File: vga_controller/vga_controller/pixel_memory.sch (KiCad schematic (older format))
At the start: 7 parts, among them J1 DB15_Female_HighDensity

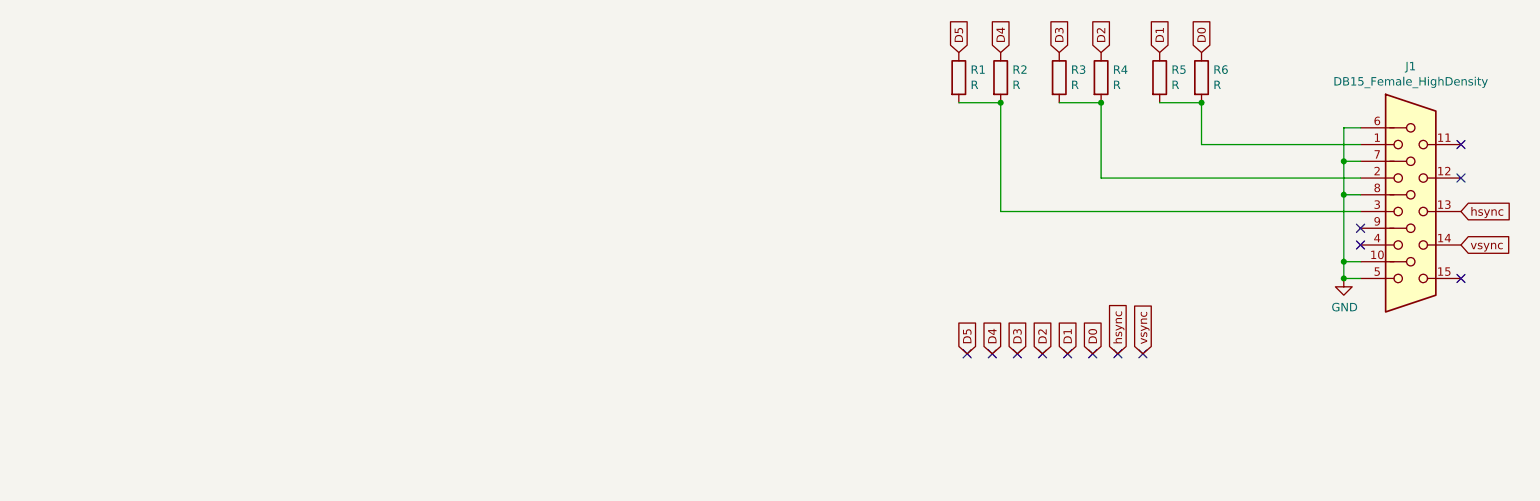
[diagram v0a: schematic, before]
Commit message: made interconnections between sheets
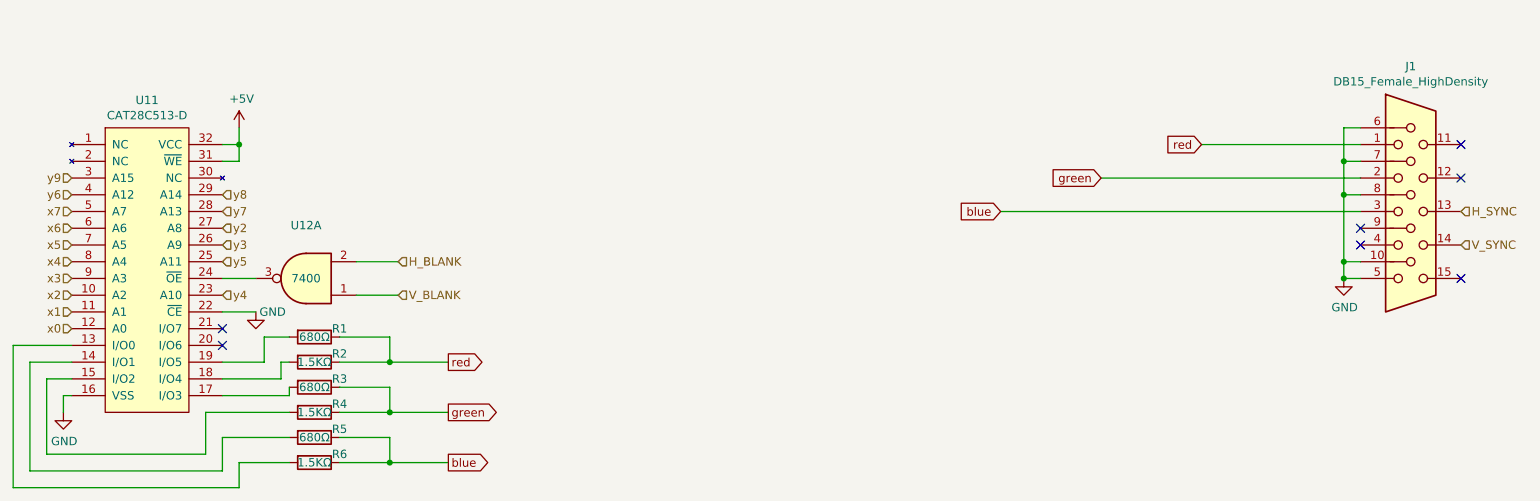
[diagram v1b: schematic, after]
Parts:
- added U11: CAT28C513-D, Package_DIP:DIP-32_W7.62mm, symbol vga_controller-rescue:CAT28C513-D-parallel_eeprom
- added U12: 7400, symbol 74xx:7400
- R1, R3, R5: value R -> 680Ω
- R2, R4, R6: value R -> 1.5KΩ
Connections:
- net D1 is gone; now on net blue: R5.1
- net D3 is gone; now on net green: R3.1
- net D5 is gone; now on net red: R1.1
- net GND: now also U11.16 (VSS), U11.22 (~CE)
- net D0 renamed blue
- net blue: now also J1.3
- net D2 renamed green
- net green: now also J1.2
- net D4 renamed red
- net red: now also J1.1
- net hsync renamed H_SYNC
- net vsync renamed V_SYNC
- new net: R6.2, U11.13 (I/O0)
- new net: R5.2, U11.14 (I/O1)
- new net: R4.2, U11.15 (I/O2)
- new net: R3.2, U11.17 (I/O3)
- new net: R2.2, U11.18 (I/O4)
- new net: R1.2, U11.19 (I/O5)
- new net: U11.24 (~OE), U12.3
- new net +5V: U11.31 (~WE), U11.32 (VCC)
- new net H_BLANK: U12.2
- new net V_BLANK: U12.1
- new net x0: U11.12 (A0)
- new net x1: U11.11 (A1)
- new net x2: U11.10 (A2)
- new net x3: U11.9 (A3)
- new net x4: U11.8 (A4)
- new net x5: U11.7 (A5)
- new net x6: U11.6 (A6)
- new net x7: U11.5 (A7)
- new net y2: U11.27 (A8)
- new net y3: U11.26 (A9)
- new net y4: U11.23 (A10)
- new net y5: U11.25 (A11)
- new net y6: U11.4 (A12)
- new net y7: U11.28 (A13)
- new net y8: U11.29 (A14)
- new net y9: U11.3 (A15)
- no-connect marks 13 -> 7

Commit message: added routes
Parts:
- J1: footprint (none) -> Connector_Dsub:DSUB-15_Female_Horizontal_P2.77x2.54mm_EdgePinOffset9.40mm
- U12: footprint (none) -> Package_DIP:DIP-14_W7.62mm
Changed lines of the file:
@@
 F 0 "J1" H 10350 3217 50  0000 C CNN
 F 1 "DB15_Female_HighDensity" H 10350 3126 50  0000 C CNN
-F 2 "" H 9400 2750 50  0001 C CNN
+F 2 "Connector_Dsub:DSUB-15_Female_Horizontal_P2.77x2.54mm_EdgePinOffset9.40mm" H 9400 2750 50  0001 C CNN
 F 3 " ~" H 9400 2750 50  0001 C CNN
 	1    10350 2350
@@
 F 0 "U12" H 3750 2433 50  0000 C CNN
 F 1 "7400" H 3750 2750 50  0000 C CNN
-F 2 "" H 3750 2750 50  0001 C CNN
+F 2 "Package_DIP:DIP-14_W7.62mm" H 3750 2750 50  0001 C CNN
 F 3 "http://www.ti.com/lit/gpn/sn7400" H 3750 2750 50  0001 C CNN
 	1    3750 2750
